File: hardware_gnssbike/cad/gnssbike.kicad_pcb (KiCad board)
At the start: 4 copper layers, 34 x 90 mm, 131 parts, among them J101 HRO TYPE-C-31-M-12, J102 JST SM06B-GHS-TB, J103 JST S4B-ZR-SM4A-TF, J201 Tag-Connect TC2030-NL, J302 Hirose U.FL-R-SMT-1, J401 Hirose FH28-10S-0.5SH, J402 Molex 503480-0500, Q401 DMG1012T-7, Q601 DMG1012T-7, Q602 DMG1012T-7, Q603 DMG1012T-7, SW601 Omron B3S-1002P, SW602 Omron B3S-1002P, SW603 Omron B3S-1002P, U101 nPM1300-QEAA, U102 MAX17262REWL, U103 AEM10900, U104 TPS7A0218PDQN, U201 MinewSemi ME54BS13, U301 u-blox MAX-F10S, U302 TI TXU0204BQAR, U501 MX25R6435F, U502 Bosch BMP585, U503 Bosch BMI270, U504 MMC5633NJL, U505 TI OPT3001DNPR

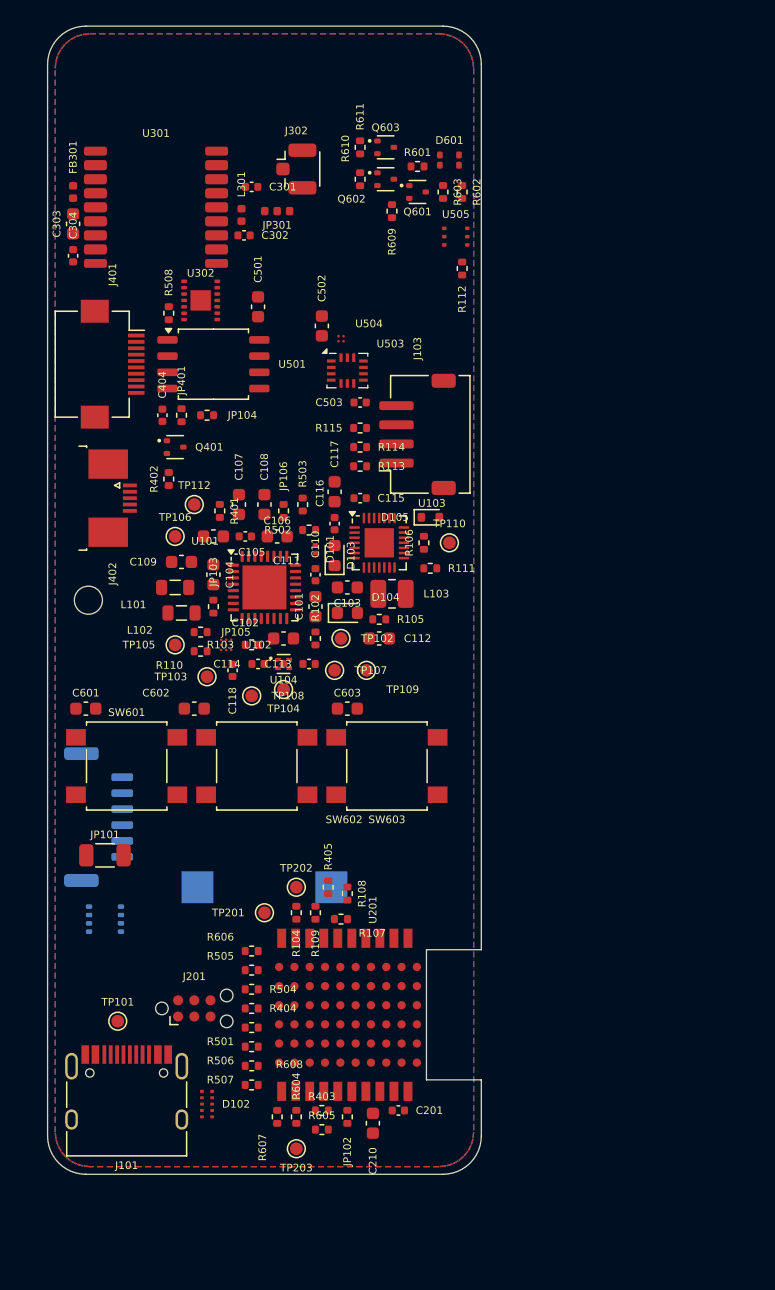
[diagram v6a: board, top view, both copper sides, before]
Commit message: feat(hardware): the four parts LCSC forced out, drawn from their drawings
The switch, the buzzer, the RGB LED and the magnetometer all had to
change, and each one came back from its drawing with something the
catalogue does not say.

  SW601..603  Omron B3S-1002P -> XunPu TS-1088R-02026 (C455280). It has
        TWO terminals, not four, so the land pattern is new even though
        the schematic already treated the key as two ends. Body 3,90 x
        3,00 x 2,00 against 6,6 x 6 x 3,4, which frees half the area the
        three keys took on the edge, and 260 gf against 230 - firmer,
        which is what gloves want. But the plunger rises only 0,50 mm
        above the steel cap against the Omron's 0,7, and the keys are
        pressed through the case: the case plunger changes.

  LS601  Same Sky CPT-1117-83-SMT (ONE in stock) -> Murata
        PKLCS1212E4001-R1 (C113159), the only substitute that keeps the
        84 dB. At 25 km/h with wind, the 65 to 70 dB of the 9 x 9 parts
        is inaudible, and an inaudible buzzer is no buzzer. The drawing
        corrects two things the catalogue hides: the sound hole is a
        LATERAL slot of 1,9 x 0,9 mm whose lower edge sits 0,30 mm off
        the board, with a channel underneath leaving by the opposite
        wall - so the case needs a side duct, not a hole in the lid -
        and the body is uniform dark graphite, with gold terminals, not
        black with a pale top. It also asks for 1 k to 2 k in series and
        forbids DC, which R607 and R608 now have to be checked against.

  D601  Kingbright APTF1616 (the suffix no longer exists, and what does
        has 305 pieces) -> TUOZHAN S4-3528RGBTA-A (C2827321), 2 million
        in stock at a twentieth of the price, common anode as the design
        wants. It is 3,5 x 2,8 instead of 1,6 x 1,6, so the LED zone had
        to widen and the part moved down 0,6 mm: at 1,9 mm tall it stood
        3,25 mm from the light sensor, which asks for twice a
        ne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
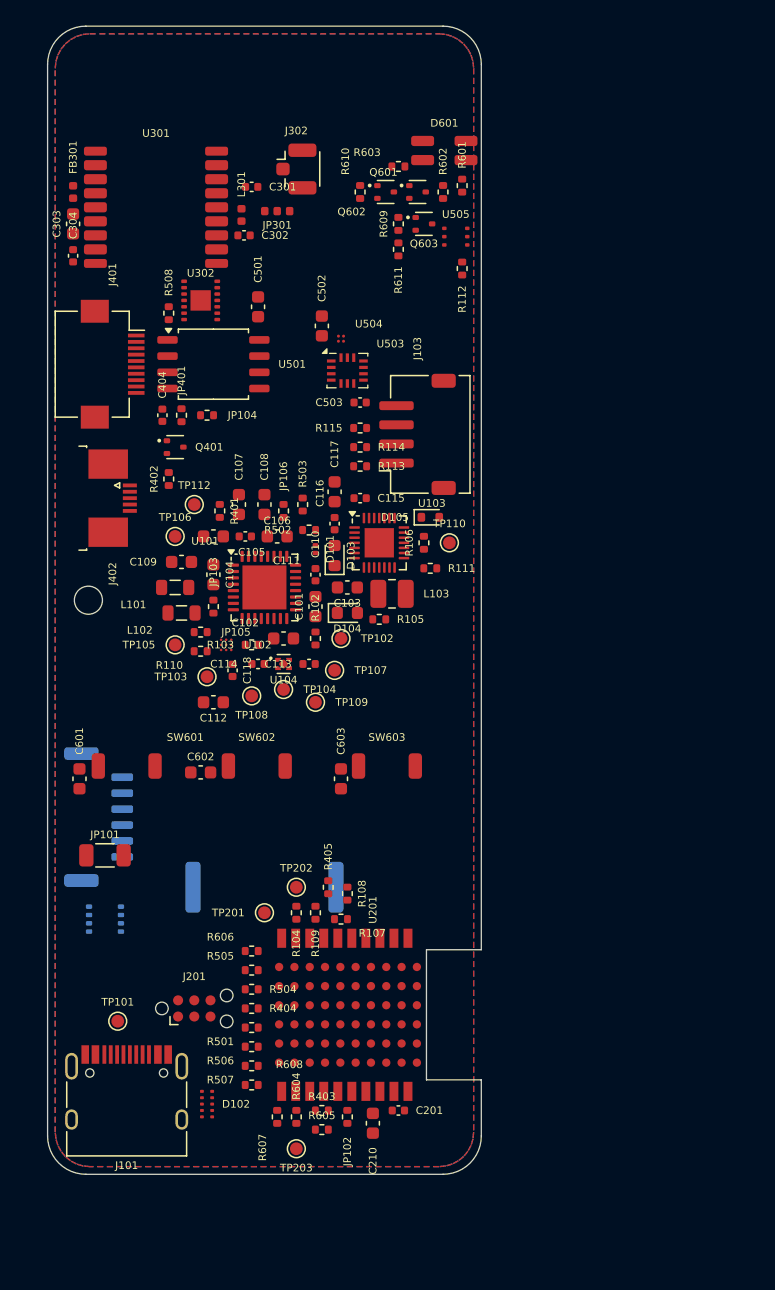
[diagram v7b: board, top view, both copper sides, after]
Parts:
- D601: value APTF1616SEEZGKQBKC -> TUOZHAN S4-3528RGBTA-A; footprint gnssbike:LED_RGB_APTF1616_1.6x1.6mm -> gnssbike:LED_RGB_3528_3.5x2.8mm
- LS601: value CPT-1117-83-SMT -> Murata PKLCS1212E4001-R1; footprint gnssbike:Buzzer_CPT-1117-83-SMT_11x9mm -> gnssbike:Buzzer_PKLCS1212E4001_12x12mm
- SW601, SW602, SW603: value Omron B3S-1002P -> XunPu TS-1088R-02026; footprint Button_Switch_SMD:SW_SPST_B3S-1000 -> gnssbike:SW_TS-1088R_3.9x3mm
- U504: value MMC5633NJL -> Memsic MMC5603NJ; footprint gnssbike:MMC5633_WLP-4_0.85x0.85mm -> gnssbike:MMC5603_WLP-4_0.82x0.82mm
- moved C112 13.9 mm to (38.0, 78.0)
- moved R611 8.54 mm to (52.5, 42.5)
- moved Q603 6.71 mm to (54.5, 40.5)
- moved C601 5.52 mm to (27.5, 84.0), turned to 90 degrees
- moved C603 5.52 mm to (48.0, 84.0), turned to 90 degrees
- moved C602 5.02 mm to (37.0, 83.5)
- moved TP109 4.72 mm to (46.0, 78.0)
- moved R603 4.03 mm to (52.5, 36.0), turned to 0 degrees
- moved R601 3.81 mm to (57.5, 37.5), turned to 90 degrees
- moved R602 1.50 mm to (56.0, 38.0)
- moved R609 1.12 mm to (52.5, 40.5)
- moved Q602 1.00 mm to (51.5, 38.0)
- moved R610 1.00 mm to (49.5, 38.0)
- moved D601 0.85 mm to (56.1, 34.8)

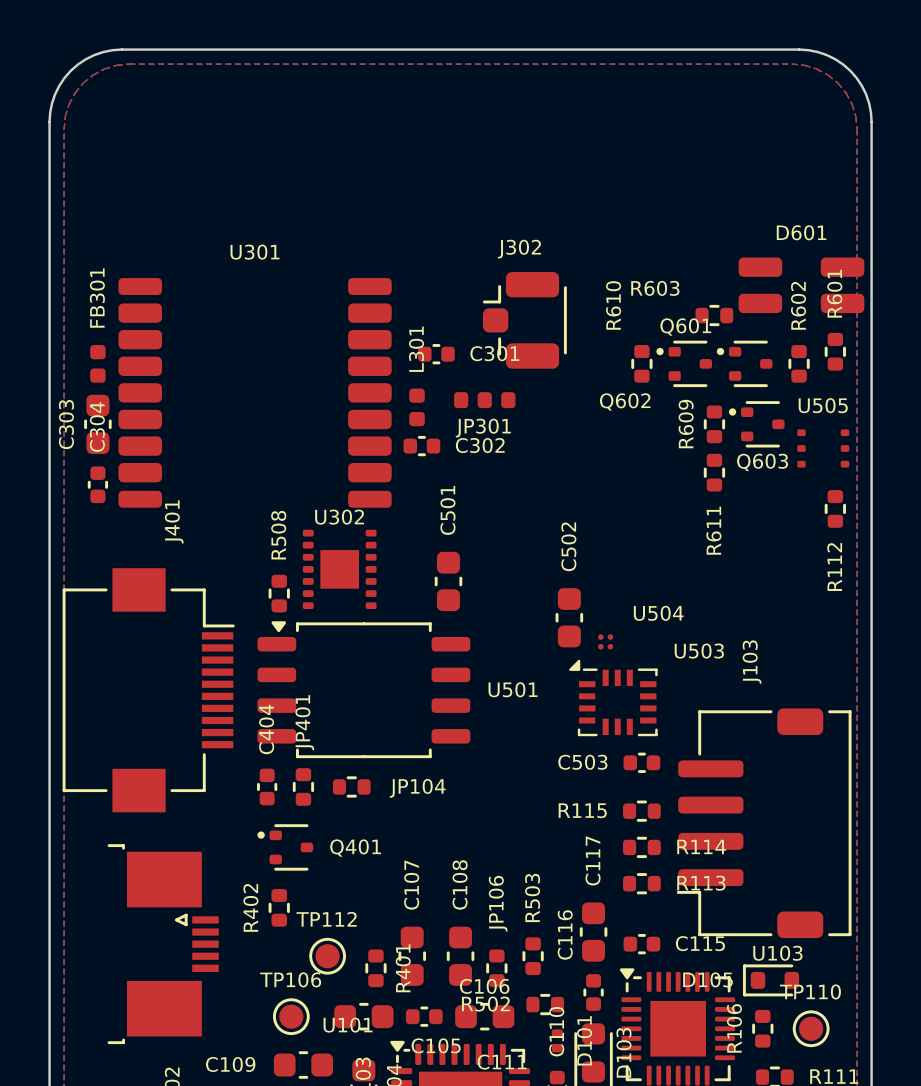
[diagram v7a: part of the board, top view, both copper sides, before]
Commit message: feat(hardware): the GNSS antenna comes onto the board, and the cut-out shrinks
The TE L000670-01 is zero at LCSC, and it was never going to work here
anyway: it asked for 40,5 x 14,5 mm with no copper on ANY layer, which is
wider than this whole 34 mm board, and its own efficiency curve collapsed
with a short ground plane - 62 % in L5 at 90 mm of ground, 43 % at 70,
29 % at 50. L5 is the entire reason the MAX-F10S was chosen.

The Unictron H2UJ4U1H2Q0100 (C6569550, 5.491 in stock) replaces it. Its
cut-out is 15,00 x 9,35 mm on the top layer and 15,00 x 9,88 on the
bottom, measured from the BOARD EDGE, and the part is 5,0 x 3,0 x 0,5 mm
against 14 x 10,75 x 1.

E301 was the only part still living outside the board: it had no
footprint, so the jumper's CHIP branch went to something that was not
laid out. It now has a land pattern read off the layout guide - two
ground/tuning pads of 0,80 x 2,98 straddling the ends, 0,40 under the
body and 0,40 outside for the fillet to climb the wrap-around
metallisation, and a 1,00 x 2,00 signal pad at the geometric centre -
and it sits on the bottom edge, 0,30 mm from it.

Its two end pads are ground AND tuning: they reach the plane through
C305 and C306, positions [8] and [9] of the data sheet's network, not
directly. The matching network's values changed with the antenna: the
shunt is 1,5 pF, the series element becomes a 3,6 pF CAPACITOR instead
of a 3,9 nH inductor, and the second shunt is not fitted. Same 0402
land patterns, so the board does not change - only what is soldered on
it, and it changes again if the u.FL branch is the one fitted.

The cut-out is 20,08 mm wide and not the data sheet's 15,00, and that is
deliberate: the cut-out is asymmetric about the antenna - 2,46 mm one
side and 7,54 the other - and which side is which is not determined.
Applying 7,54 to both sides meets the requirement whichever way the part
faces. It costs about 5 mm of ground plane on an antenna that depends on
it, and it can go back to 15,00 onc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
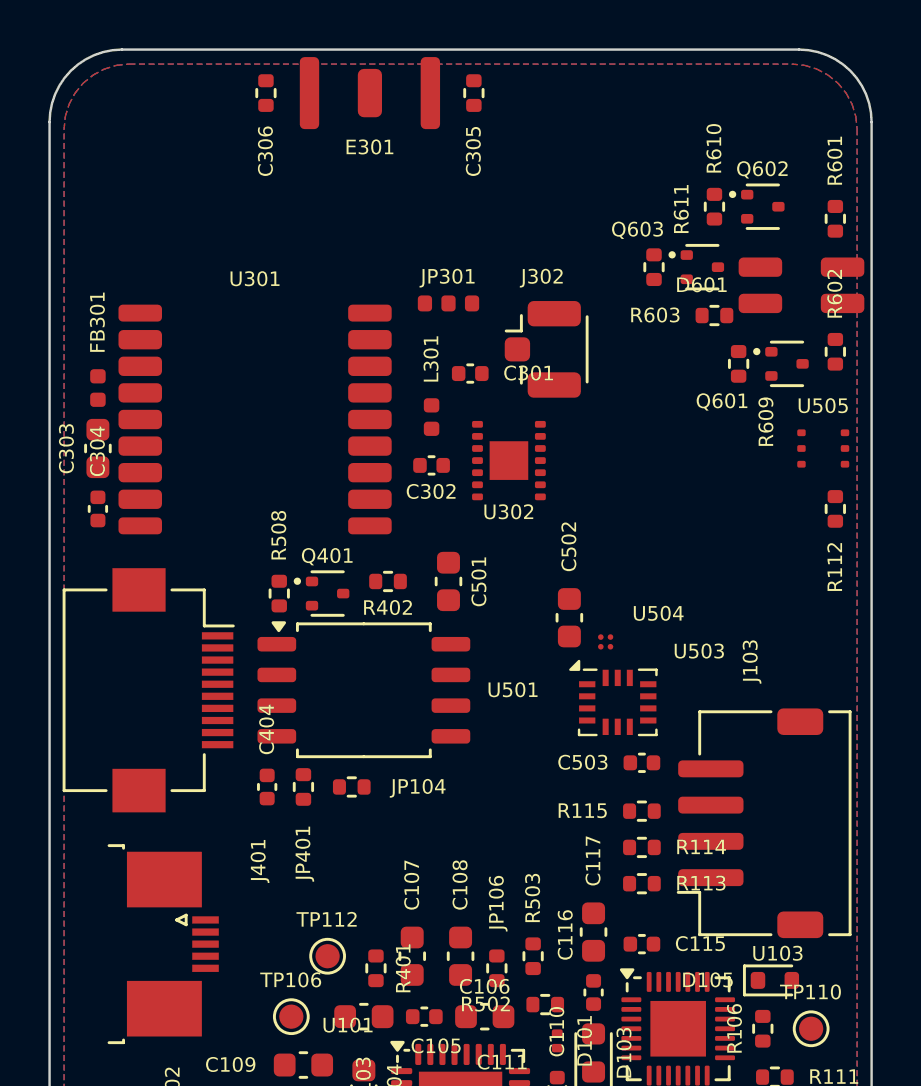
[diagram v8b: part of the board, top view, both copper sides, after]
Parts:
- added C305: 2,7 pF, Resistor_SMD:R_0402_1005Metric, F.Cu at (42.5, 26.8)
- added C306: 6,8 pF, Resistor_SMD:R_0402_1005Metric, F.Cu at (34.0, 26.8)
- added E301: Unictron H2UJ4U1H2Q0100, gnssbike:Antena_Unictron_H2UJ4U1H2Q0100_5x3mm, F.Cu at (38.2, 26.8)
- C301: value 2,2 pF -> 1,5 pF
- C302: value 2,2 pF -> NP
- J401: value Hirose FH28-10S-0.5SH -> Hirose FH12-10S-0.5SH(55)
- L301: value 3,9 nH -> 3,6 pF
- moved R402 14.2 mm to (39.0, 47.0), turned to 0 degrees
- moved Q401 10.6 mm to (36.5, 47.5)
- moved R611 8.86 mm to (50.0, 34.0)
- moved U302 8.32 mm to (44.0, 42.0)
- moved Q602 7.16 mm to (54.5, 31.5)
- moved R610 7.16 mm to (52.5, 31.5)
- moved Q603 6.96 mm to (52.0, 34.0)
- moved R601 5.50 mm to (57.5, 32.0)
- moved JP301 4.27 mm to (41.5, 35.5)
- moved R609 2.69 mm to (53.5, 38.0)
- moved C301 1.61 mm to (42.4, 38.4)
- moved R602 1.58 mm to (57.5, 37.5)
- moved Q601 1.50 mm to (55.5, 38.0)
- moved J302 1.50 mm to (45.4, 37.4)
- moved U301 1.10 mm to (33.5, 40.3)
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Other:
- board text added: "133 pecas colocadas, 7 fora da placa (painel, antena e modulos solares vivem na caixa)"
- board text removed: "130 pecas colocadas, 8 fora da placa (painel, antena e modulos solares vivem na caixa)"
